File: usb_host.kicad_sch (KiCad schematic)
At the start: 2 parts, among them J8 USB_A_Stacked, U6 INA219AxD

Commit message: More USB schematic work
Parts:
- added ACTIVE, PORT1, PORT2, PORT3, PORT4: LED_Small, symbol Device:LED_Small
- added C46, C47, C50, C51, C52, C53: 10uF, symbol Device:C_Small
- added C48, C49: 100nF, symbol Device:C_Small
- added J13: USB_A_Stacked, symbol Connector:USB_A_Stacked
- added R16, R17: 220, symbol Device:R_Small
- added R18: 470, symbol Device:R_Small
- added R19: 0.1/1% PT2512K 070R1L, symbol Device:R
- added R20: 4.7K, symbol Device:R_Small
- added R21, R22, R23: 10K, symbol Device:R_Small
- added U7: CH334F, Package_DFN_QFN:QFN-24-1EP_4x4mm_P0.5mm_EP2.7x2.7mm, symbol Interface_USB:CH334F
- added U8, U9: MT9700_SY6280, Package_TO_SOT_SMD:SOT-23-5, symbol GenericJLC:MT9700_SY6280
- added Y3: 12MHz, symbol Device:Crystal_Small
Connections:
- net USB+: now also U7.15 (DPU+)
- net USB-: now also U7.14 (DMU-)
- net GND: now reaches U6.1 (A1)
- net GND: now also J8.4 (GND1), J8.8 (GND2), J8.SH (Shield), U6.2 (A0), U6.6 (GND), C46.2, C47.2, C48.2, C49.2, C52.2, C53.2, J13.4 (GND1), J13.8 (GND2), J13.SH (Shield), R20.2, R21.2, R22.2, R23.2, U7.25 (GND), U8.2 (GND), U9.2 (GND)
- net SDA: now reaches U6.3 (SDA)
- net SCL: now reaches U6.4 (SCL)
- net SWITCHED_3V3: now reaches U6.5 (VS)
- net SWITCHED_3V3: now also ACTIVE.2 (A), C46.1, C48.1, C49.1, U7.20 (VDD33_{LDO}), U8.1 (OUT)
- net USB_VBUS: now reaches U6.7 (IN-)
- net USB_VBUS: now also J8.1 (VBUS1), J8.5 (VBUS2), J13.1 (VBUS1), J13.5 (VBUS2), R19.2
- net SWITCHED_5V: now reaches U6.8 (IN+)
- net SWITCHED_5V: now also C47.1, R19.1, U7.19 (V5), U9.1 (OUT)
- net D3-: now reaches J8.2 (D1-)
- net D3-: now also U7.7 (DM3-)
- net D3+: now reaches J8.3 (D1+)
- net D3+: now also U7.8 (DP3+)
- net D4-: now reaches J8.6 (D2-)
- net D4-: now also U7.5 (DM4-)
- net D4+: now reaches J8.7 (D2+)
- net D4+: now also U7.6 (DP4+)
- new net: R21.1, U8.3 (SET)
- new net: PORT3.2 (A), PORT4.1 (K), R16.2
- new net: PORT1.2 (A), PORT2.1 (K), R17.2
- new net: ACTIVE.1 (K), R18.2
- new net: U7.3 (XO), Y3.1
- new net: U7.4 (XI), Y3.2
- new net: R20.1, U9.3 (SET)
- new net +3.3V: C53.1, U8.5 (IN)
- new net +5V: C52.1, U9.5 (IN)
- new net D1+: J13.3 (D1+), U7.12 (DP1+)
- new net D1-: J13.2 (D1-), U7.11 (DM1-)
- new net D2+: J13.7 (D2+), U7.10 (DP2+)
- new net D2-: J13.6 (D2-), U7.9 (DM2-)
- new net LED1: R16.1, U7.22 (LED1)
- new net LED2: R17.1, U7.23 (LED2)
- new net LED4: PORT1.1 (K), PORT2.2 (A), PORT3.1 (K), PORT4.2 (A), R18.1, U7.21 (LED4/SDA)
- new net POWER_ON: R22.1, R23.1, U8.4 (ON), U9.4 (ON)
- no-connect marks 0 -> 5
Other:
- note added: "6.8k/10k = 0.6A"
- note added: "6.8k/4.7k = 1.4A"
- moved on the sheet: J8

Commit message: Getting close. Fault circuit left
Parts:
- removed J8: USB_A_Stacked, symbol Connector:USB_A_Stacked
- added J18: Conn_02x05_Odd_Even, Connector_PinHeader_2.54mm:PinHeader_2x05_P2.54mm_Vertical, symbol Connector_Generic:Conn_02x05_Odd_Even
- ACTIVE1: renamed from ACTIVE; footprint (none) -> LED_SMD:LED_0603_1608Metric
- C46, C47, C50, C51, C52, C53: footprint (none) -> Capacitor_SMD:C_0603_1608Metric
- C48, C49: footprint (none) -> Capacitor_SMD:C_0402_1005Metric
- J13: footprint (none) -> Connector_USB:USB_A_Wuerth_61400826021_Horizontal_Stacked
- PORT1, PORT2, PORT3, PORT4: footprint (none) -> LED_SMD:LED_0603_1608Metric
- R16, R17, R18, R20, R21, R22, R23: footprint (none) -> Resistor_SMD:R_0402_1005Metric
- R19: footprint (none) -> Resistor_SMD:R_2512_6332Metric
- Y3: footprint (none) -> Crystal:Crystal_SMD_3225-4Pin_3.2x2.5mm
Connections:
- net D3+: now also J18.5 (Pin_5)
- net D3-: now also J18.3 (Pin_3)
- net D4+: now also J18.6 (Pin_6)
- net D4-: now also J18.4 (Pin_4)
- net GND: now also C50.2, J18.10 (Pin_10), J18.7 (Pin_7), J18.8 (Pin_8)
- net SWITCHED_3V3: now also C50.1
- net USB_VBUS: now also J18.1 (Pin_1), J18.2 (Pin_2)
- no-connect marks 5 -> 6
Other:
- note added: "Motherboard Layout"

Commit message: Pack things in
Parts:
- removed Y3: 12MHz, Crystal:Crystal_SMD_3225-4Pin_3.2x2.5mm, symbol Device:Crystal_Small
- added Y3: 12MHz, symbol Device:Crystal_GND24_Small
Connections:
- net GND: now also C51.2, Y3.2 (G), Y3.4 (G)
- net SWITCHED_5V: now also C51.1
- net at U7.3 (XO): now also Y3.1
- net at U7.4 (XI): now also Y3.3
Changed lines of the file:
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@@
+	(wire
+		(pts
+			(xy 50.8 30.48) (xy 58.42 30.48)
+		)
+		(stroke
+			(width 0)
+			(type default)
+		)
+	)
 	(wire
 		(pts
@@
 	)
 	(symbol
+		(lib_id "power:GND")
+		(at 71.12 130.81 0)
+		(unit 1)
+		(body_style 1)
+		(exclude_from_sim no)
+		(in_bom yes)
+		(on_board yes)
+		(in_pos_files yes)
+		(dnp no)
+		(fields_autoplaced yes)
+		(property "Reference" "#PWR0124"
+			(at 71.12 137.16 0)
+			(hide yes)
+			(show_name no)
+			(do_not_autoplace no)
+			(effects
+				(font
+					(size 1.27 1.27)
+				)
+			)
+		)
+		(property "Value" "GND"
+			(at 71.12 135.89 0)
+			(show_name no)
+			(do_not_autoplace no)
+			(effects
+				(font
+					(size 1.27 1.27)
+				)
+			)
+		)
+		(property "Footprint" ""
+			(at 71.12 130.81 0)
+			(hide yes)
+			(show_name no)
+			(do_not_autoplace no)
+			(effects
+				(font
+					(size 1.27 1.27)
+				)
+			)
+		)
+		(property "Datasheet" ""
+			(at 71.12 130.81 0)
+			(hide yes)
+			(show_name no)
+			(do_not_autoplace no)
+			(effects
+				(font
+					(size 1.27 1.27)
+				)
+			)
+		)
+		(property "Description" "Power symbol creates a global label with name \"GND\" , ground"
+			(at 71.12 130.81 0)
+			(hide yes)
+			(show_name no)
+			(do_not_autoplace no)
+			(effects
+				(font
+					(size 1.27 1.27)
+				)
+			)
+		)
+		(pin "1"
+		)
+		(instances
+			(project "p4hil"
+				(path "/b29b188c-1e37-42da-9ef2-78e9f87e21db/d964722f-0742-41bf-972a-222da90a91eb"
+					(reference "#PWR0124")
+					(unit 1)
+				)
+			)
+		)
+	)
+	(symbol
 		(lib_id "Device:R_Small")
 		(at 26.67 38.1 0)
@@
 	)
 	(symbol
+		(lib_id "Device:Crystal_GND24_Small")
+		(at 71.12 128.27 0)
+		(unit 1)
+		(body_style 1)
+		(exclude_from_sim no)
+		(in_bom yes)
+		(on_board yes)
+		(in_pos_files yes)
+		(dnp no)
+		(fields_autoplaced yes)
+		(property "Reference" "Y3"
+			(at 71.12 121.92 0)
+			(show_name no)
+			(do_not_autoplace no)
+			(effects
+				(font
+					(size 1.27 1.27)
+				)
+			)
+		)
+		(property "Value" "12MHz"
+			(at 71.12 124.46 0)
+			(show_name no)
+			(do_not_autoplace no)
+			(effects
+				(font
+					(size 1.27 1.27)
+				)
+			)
+		)
+		(property "Footprint" ""
+			(at 71.12 128.27 0)
+			(hide yes)
+			(show_name no)
+			(do_not_autoplace no)
+			(effects
+				(font
+					(size 1.27 1.27)
+				)
+			)
+		)
+		(property "Datasheet" ""
+			(at 71.12 128.27 0)
+			(hide yes)
+			(show_name no)
+			(do_not_autoplace no)
+			(effects
+				(font
+					(size 1.27 1.27)
+				)
+			)
+		)
+		(property "Description" "Four pin crystal, GND on pins 2 and 4, small symbol"
+			(at 71.12 128.27 0)
+			(hide yes)
+			(show_name no)
+			(do_not_autoplace no)
+			(effects
+				(font
+					(size 1.27 1.27)
+				)
+			)
+		)
+		(property private "KLC_S3.3" "The rectangle is not a symbol body but a graphical element"
+			(at 71.12 138.43 0)
+			(hide yes)
+			(show_name yes)
+			(do_not_autoplace no)
+			(effects
+				(font
+					(size 1.27 1.27)
+				)
+			)
+		)
+		(property private "KLC_S4.1" "Some pins are on 50mil grid to make the symbol small"
+			(at 71.12 140.97 0)
+			(hide yes)
+			(show_name yes)
+			(do_not_autoplace no)
+			(effects
+				(font
+					(size 1.27 1.27)
+				)
+			)
+		)
+		(pin "2"
+		)
+		(pin "1"
+		)
+		(pin "3"
+		)
+		(pin "4"
+		)
+		(instances
+			(project "p4hil"
+				(path "/b29b188c-1e37-42da-9ef2-78e9f87e21db/d964722f-0742-41bf-972a-222da90a91eb"
+					(reference "Y3")
+					(unit 1)
+				)
+			)
+		)
+	)
+	(symbol
 		(lib_id "power:GND")
 		(at 152.4 67.31 0)
@@
 	)
 	(symbol
+		(lib_id "power:GND")
+		(at 58.42 35.56 0)
+		(unit 1)
+		(body_style 1)
+		(exclude_from_sim no)
+		(in_bom yes)
+		(on_board yes)
+		(in_pos_files yes)
+		(dnp no)
+		(fields_autoplaced yes)
+		(property "Reference" "#PWR0123"
+			(at 58.42 41.91 0)
+			(hide yes)
+			(show_name no)
+			(do_not_autoplace no)
+			(effects
+				(font
+					(size 1.27 1.27)
+				)
+			)
+		)
+		(property "Value" "GND"
+			(at 58.42 40.64 0)
+			(show_name no)
+			(do_not_autoplace no)
+			(effects
+				(font
+					(size 1.27 1.27)
+				)
+			)
+		)
+		(property "Footprint" ""
+			(at 58.42 35.56 0)
+			(hide yes)
+			(show_name no)
+			(do_not_autoplace no)
+			(effects
+				(font
+					(size 1.27 1.27)
+				)
+			)
+		)
+		(property "Datasheet" ""
+			(at 58.42 35.56 0)
+			(hide yes)
+			(show_name no)
+			(do_not_autoplace no)
+			(effects
+				(font
+					(size 1.27 1.27)
+				)
+			)
+		)
+		(property "Description" "Power symbol creates a global label with name \"GND\" , ground"
+			(at 58.42 35.56 0)
+			(hide yes)
+			(show_name no)
+			(do_not_autoplace no)
+			(effects
+				(font
+					(size 1.27 1.27)
+				)
+			)
+		)
+		(pin "1"
+		)
+		(instances
+			(project "p4hil"
+				(path "/b29b188c-1e37-42da-9ef2-78e9f87e21db/d964722f-0742-41bf-972a-222da90a91eb"
+					(reference "#PWR0123")
+					(unit 1)
+				)
+			)
+		)
+	)
+	(symbol
 		(lib_id "Device:C_Small")
 		(at 58.42 60.96 0)
@@
 					(unit 1)
 				)
-			)
-		)
-	)
-	(symbol
-		(lib_id "Device:Crystal_Small")
-		(at 71.12 128.27 0)
-		(unit 1)
-		(body_style 1)
-		(exclude_from_sim no)
-		(in_bom yes)
-		(on_board yes)
-		(in_pos_files yes)
-		(dnp no)
-		(property "Reference" "Y3"
-			(at 70.866 134.112 0)
-			(show_name no)
-			(do_not_autoplace no)
-			(effects
-				(font
-					(size 1.27 1.27)
-				)
-			)
-		)
-		(property "Value" "12MHz"
-			(at 71.12 131.318 0)
-			(show_name no)
-			(do_not_autoplace no)
-			(effects
-				(font
-					(size 1.27 1.27)
-				)
-			)
-		)
-		(property "Footprint" "Crystal:Crystal_SMD_3225-4Pin_3.2x2.5mm"
-			(at 71.12 128.27 0)
-			(hide yes)
-			(show_name no)
-			(do_not_autoplace no)
-			(effects
-				(font
-					(size 1.27 1.27)
-				)
-			)
-		)
-		(property "Datasheet" ""
-			(at 71.12 128.27 0)
-			(hide yes)
-			(show_name no)
-			(do_not_autoplace no)
-			(effects
-				(font
-					(size 1.27 1.27)
-				)
-			)
-		)
-		(property "Description" "Two pin crystal, small symbol"
-			(at 71.12 128.27 0)
-			(hide yes)
-			(show_name no)
-			(do_not_autoplace no)
-			(effects
-				(font
-					(size 1.27 1.27)
-				)
-			)
-		)
-		(pin "1"
-		)
-		(pin "2"
-		)
-		(instances
-			(project "p4hil"
-				(path "/b29b188c-1e37-42da-9ef2-78e9f87e21db/d964722f-0742-41bf-972a-222da90a91eb"
-					(reference "Y3")
-					(unit 1)
-				)

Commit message: Swirly gridify
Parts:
- Y3: footprint (none) -> Crystal:Crystal_SMD_3225-4Pin_3.2x2.5mm
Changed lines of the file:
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@@
 			)
 		)
-		(property "Footprint" ""
+		(property "Footprint" "Crystal:Crystal_SMD_3225-4Pin_3.2x2.5mm"
 			(at 71.12 128.27 0)
 			(hide yes)

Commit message: clean drc
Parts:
- added D9: GREEN LED, Diode_SMD:D_0603_1608Metric, symbol Device:LED_Small_Filled
- added R93: 2.2K, Resistor_SMD:R_0402_1005Metric, symbol Device:R_Small
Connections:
- net GND: now also D9.1 (K)
- net SWITCHED_3V3: now also R93.1
- new net: D9.2 (A), R93.2

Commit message: v1
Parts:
- R16, R17: value 220 -> 4.7K
- R18: value 470 -> 47K
- R93: value 2.2K -> 4.7K
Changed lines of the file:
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@@
 			)
 		)
-		(property "Value" "470"
+		(property "Value" "47K"
 			(at 167.64 135.89 90)
 			(show_name no)
@@
 			)
 		)
-		(property "Value" "220"
+		(property "Value" "4.7K"
 			(at 142.24 123.19 90)
 			(show_name no)
@@
 			)
 		)
-		(property "Value" "2.2K"
+		(property "Value" "4.7K"
 			(at 120.65 158.7499 0)
 			(show_name no)
@@
 			)
 		)
-		(property "Value" "220"
+		(property "Value" "4.7K"
 			(at 142.24 99.06 90)
 			(show_name no)

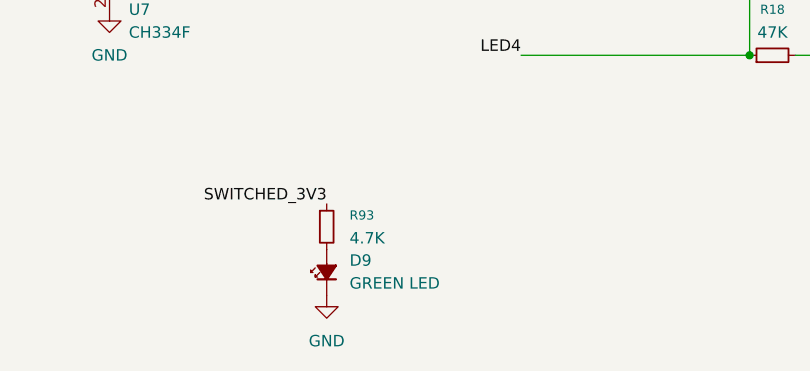
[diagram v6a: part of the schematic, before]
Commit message: Add IO expanders, swap ethernet and move USB LEDs
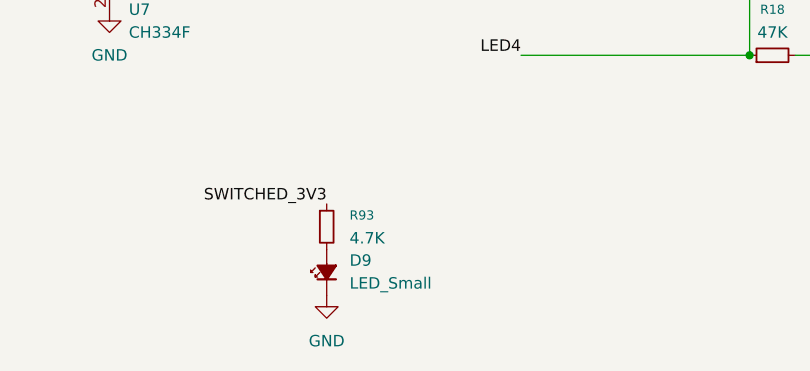
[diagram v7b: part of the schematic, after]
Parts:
- D9: value GREEN LED -> LED_Small; footprint Diode_SMD:D_0603_1608Metric -> LED_SMD:LED_0603_1608Metric
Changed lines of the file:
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@@
 			)
 		)
-		(property "Value" "GREEN LED"
+		(property "Value" "LED_Small"
 			(at 120.65 163.7664 90)
 			(show_name no)
@@
 			)
 		)
-		(property "Footprint" "Diode_SMD:D_0603_1608Metric"
+		(property "Footprint" "LED_SMD:LED_0603_1608Metric"
 			(at 118.11 162.56 90)
 			(hide yes)
